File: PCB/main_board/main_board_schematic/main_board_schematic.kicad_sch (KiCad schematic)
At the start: 15 parts, among them P1 USB_C_Plug_USB2.0, SW1 tactile_switch, U1 NCP1117-3.3_SOT223, U2 W25Q128JVS, Y1 12MHZ

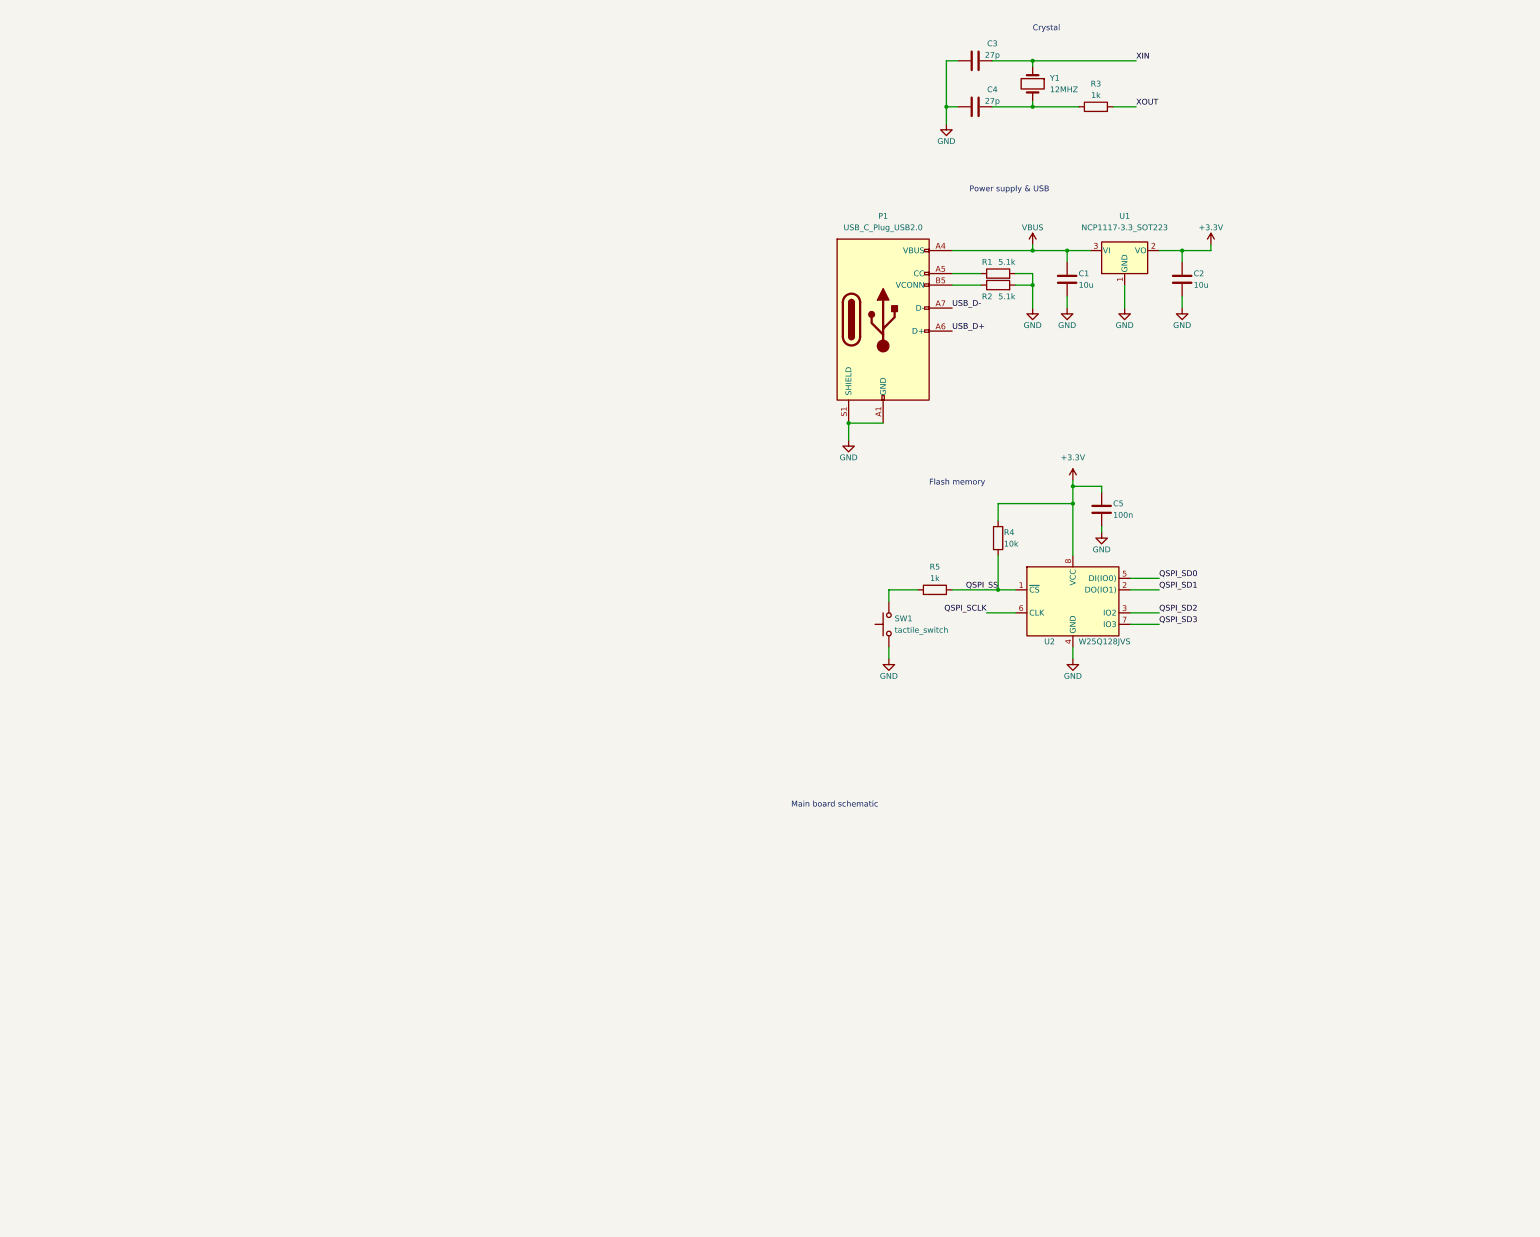
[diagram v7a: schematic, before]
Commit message: Added rp2040 alongside some components
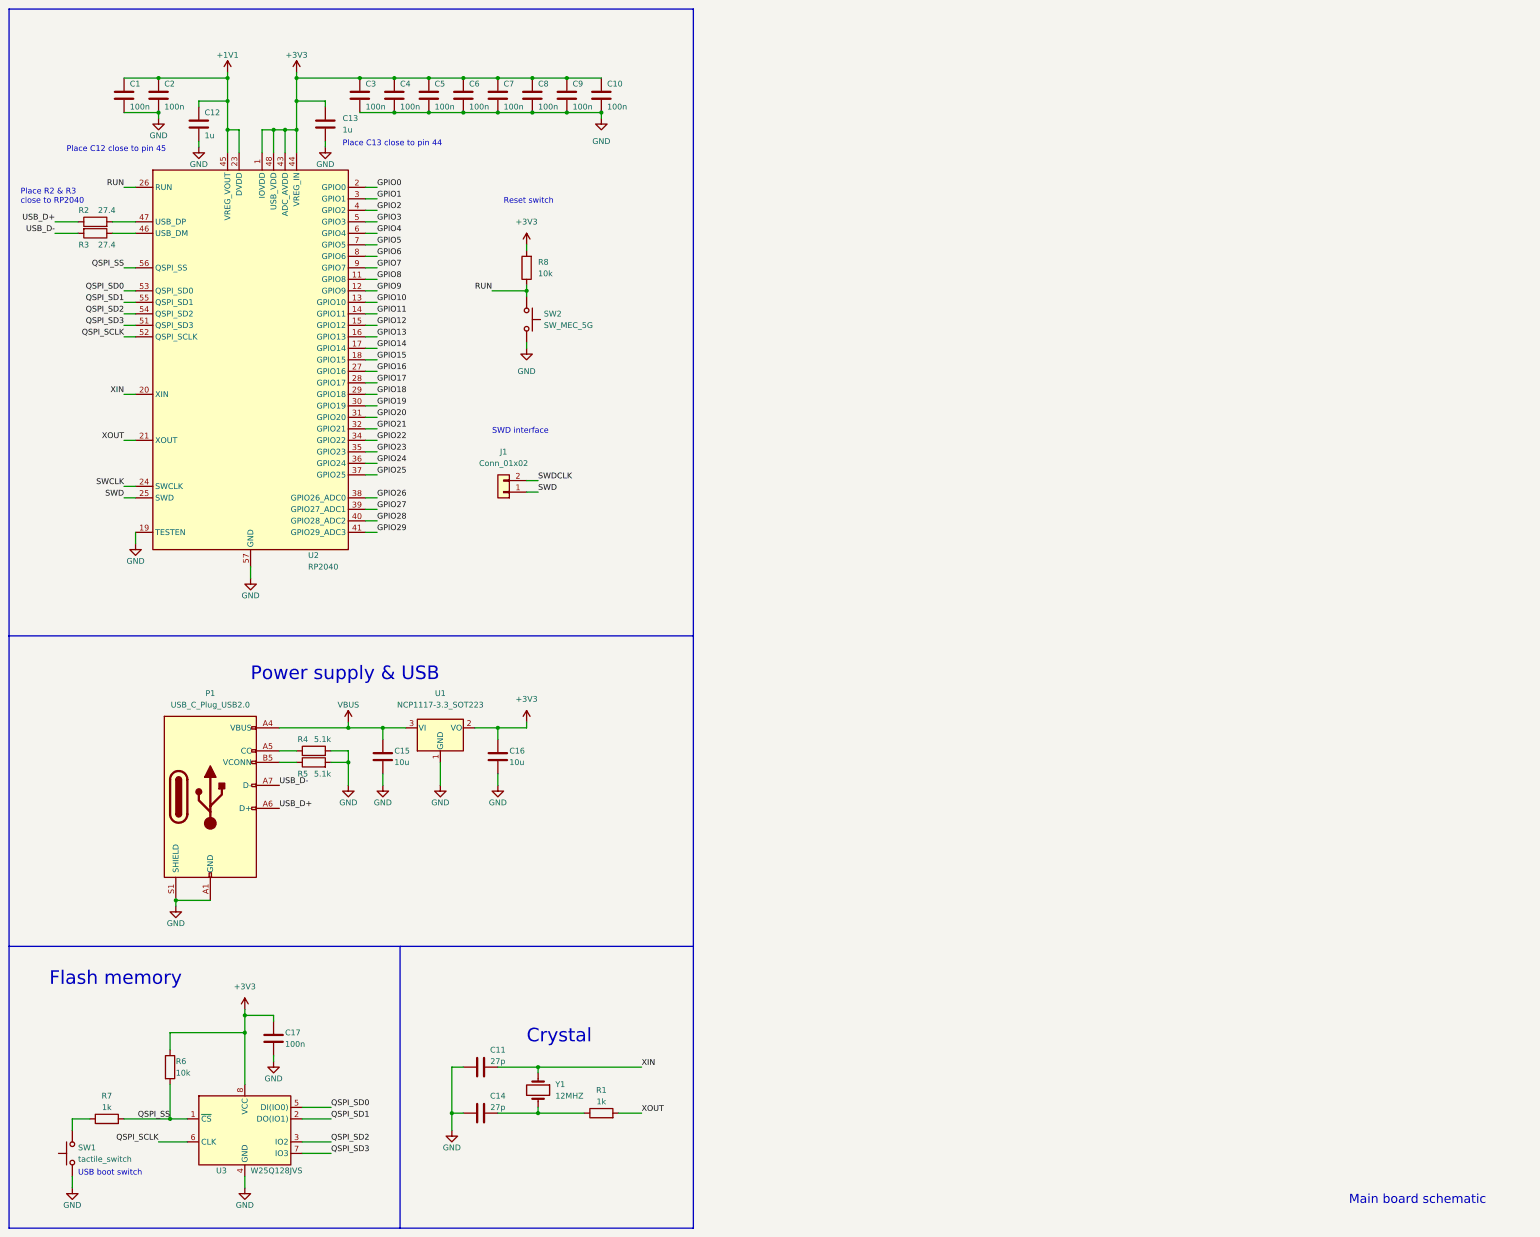
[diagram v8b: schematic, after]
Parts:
- added C1, C10, C2, C3, C4, C5, C6, C7, C8, C9: 100n, symbol Device:C
- added C12, C13: 1u, symbol Device:C
- added J1: Conn_01x02, symbol Connector_Generic:Conn_01x02
- added R2, R3: 27.4, symbol Device:R
- added R8: 10k, symbol Device:R
- added SW2: SW_MEC_5G, symbol Switch:SW_MEC_5G
- added U2: RP2040, Package_DFN_QFN:QFN-56-1EP_7x7mm_P0.4mm_EP3.2x3.2mm, symbol MCU_RaspberryPi:RP2040
- renumbered C3 to C11, C4 to C14, C1 to C15, C2 to C16, C5 to C17, R3 to R1, R1 to R4, R2 to R5, R4 to R6, R5 to R7, U2 to U3
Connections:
- net GND: now also C1.2, C10.2, C12.2, C13.2, C2.2, C3.2, C4.2, C5.2, C6.2, C7.2, C8.2, C9.2, SW2.3 (B), SW2.4 (B), U2.19 (TESTEN), U2.57 (GND)
- net QSPI_SCLK: now also U2.52 (QSPI_SCLK)
- net QSPI_SD0: now also U2.53 (QSPI_SD0)
- net QSPI_SD1: now also U2.55 (QSPI_SD1)
- net QSPI_SD2: now also U2.54 (QSPI_SD2)
- net QSPI_SD3: now also U2.51 (QSPI_SD3)
- net QSPI_SS: now also U2.56 (QSPI_SS)
- net USB_D+: now also R2.1
- net USB_D-: now also R3.2
- net XIN: now also U2.20 (XIN)
- net XOUT: now also U2.21 (XOUT)
- net +3.3V renamed +3V3
- net +3V3: now also C10.1, C13.1, C3.1, C4.1, C5.1, C6.1, C7.1, C8.1, C9.1, R8.2, U2.1 (IOVDD), U2.10 (IOVDD), U2.22 (IOVDD), U2.33 (IOVDD), U2.42 (IOVDD), U2.43 (ADC_AVDD), U2.44 (VREG_IN), U2.48 (USB_VDD), U2.49 (IOVDD)
- new net: R3.1, U2.46 (USB_DM)
- new net: R2.2, U2.47 (USB_DP)
- new net +1V1: C1.1, C12.1, C2.1, U2.23 (DVDD), U2.45 (VREG_VOUT), U2.50 (DVDD)
- new net GPIO0: U2.2 (GPIO0)
- new net GPIO1: U2.3 (GPIO1)
- new net GPIO10: U2.13 (GPIO10)
- new net GPIO11: U2.14 (GPIO11)
- new net GPIO12: U2.15 (GPIO12)
- new net GPIO13: U2.16 (GPIO13)
- new net GPIO14: U2.17 (GPIO14)
- new net GPIO15: U2.18 (GPIO15)
- new net GPIO16: U2.27 (GPIO16)
- new net GPIO17: U2.28 (GPIO17)
- new net GPIO18: U2.29 (GPIO18)
- new net GPIO19: U2.30 (GPIO19)
- new net GPIO2: U2.4 (GPIO2)
- new net GPIO20: U2.31 (GPIO20)
- new net GPIO21: U2.32 (GPIO21)
- new net GPIO22: U2.34 (GPIO22)
- new net GPIO23: U2.35 (GPIO23)
- new net GPIO24: U2.36 (GPIO24)
- new net GPIO25: U2.37 (GPIO25)
- new net GPIO26: U2.38 (GPIO26_ADC0)
- new net GPIO27: U2.39 (GPIO27_ADC1)
- new net GPIO28: U2.40 (GPIO28_ADC2)
- new net GPIO29: U2.41 (GPIO29_ADC3)
- new net GPIO3: U2.5 (GPIO3)
- new net GPIO4: U2.6 (GPIO4)
- new net GPIO5: U2.7 (GPIO5)
- new net GPIO6: U2.8 (GPIO6)
- new net GPIO7: U2.9 (GPIO7)
- new net GPIO8: U2.11 (GPIO8)
- new net GPIO9: U2.12 (GPIO9)
- new net RUN: R8.1, SW2.1 (A), SW2.2 (A), U2.26 (RUN)
- new net SWCLK: U2.24 (SWCLK)
- new net SWD: J1.1 (Pin_1), U2.25 (SWD)
- new net SWDCLK: J1.2 (Pin_2)
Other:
- note added: "Place C12 close to pin 45"
- note added: "Place C13 close to pin 44"
- note added: "Place R2 & R3 close to RP2040"
- note added: "Reset switch"
- note added: "SWD interface"
- note added: "USB boot switch"
- moved on the sheet: C11, C14, C15, C16, C17, P1, R1, R4, R5, R6, R7, SW1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
